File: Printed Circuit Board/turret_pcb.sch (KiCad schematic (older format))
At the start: 19 parts

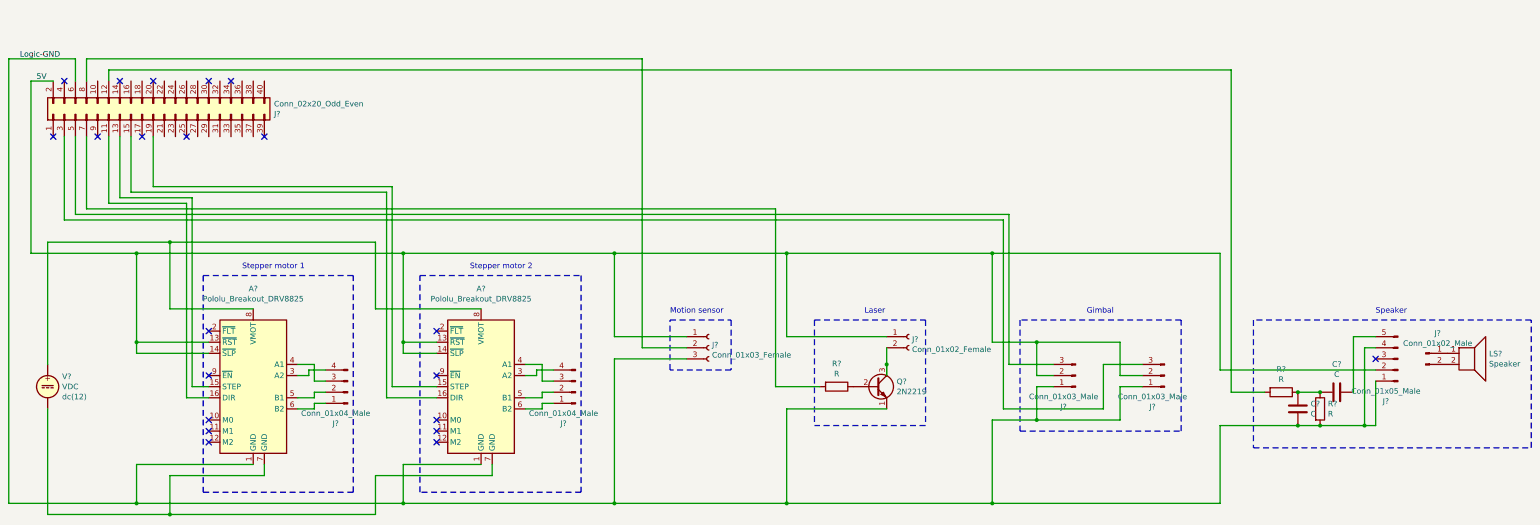
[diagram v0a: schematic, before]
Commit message: PCB separate schemas for components
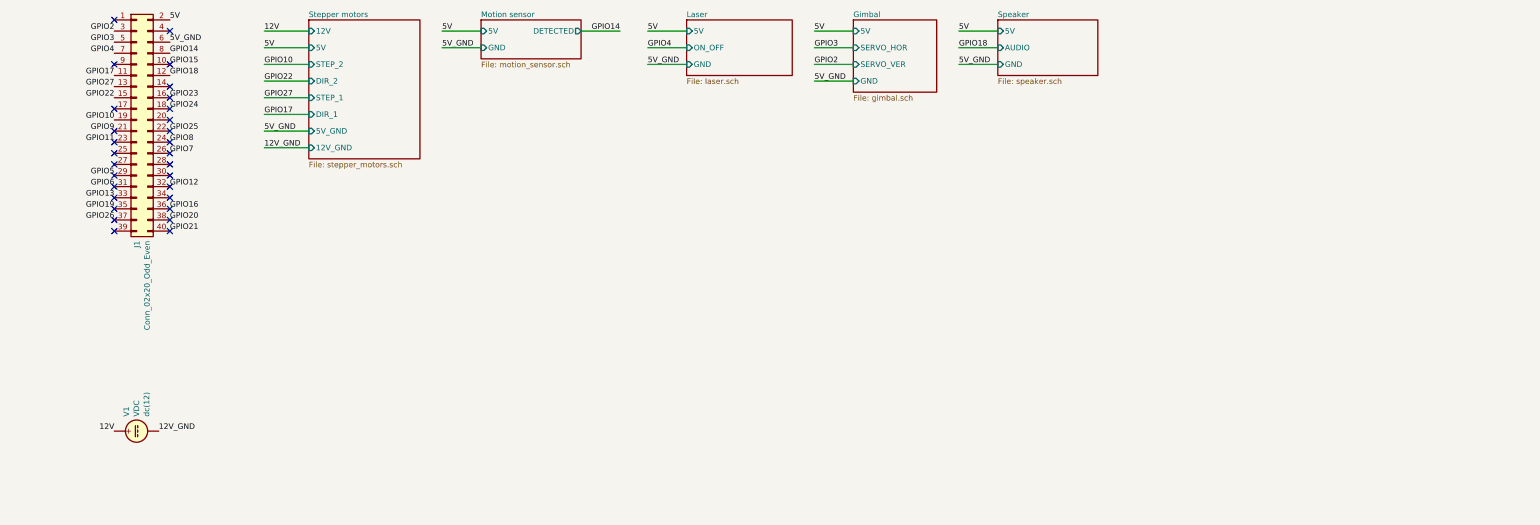
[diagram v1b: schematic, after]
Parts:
- removed A? (x2): Pololu_Breakout_DRV8825, Module:Pololu_Breakout-16_15.2x20.3mm, symbol Driver_Motor:Pololu_Breakout_DRV8825
- removed C? (x2): C, symbol Device:C
- removed J?: Conn_01x03_Female, symbol Connector:Conn_01x03_Female
- removed J? (x2): Conn_01x04_Male, symbol Connector:Conn_01x04_Male
- removed J?: Conn_01x02_Female, symbol Connector:Conn_01x02_Female
- removed J? (x2): Conn_01x03_Male, symbol Connector:Conn_01x03_Male
- removed J?: Conn_01x05_Male, symbol Connector:Conn_01x05_Male
- removed J?: Conn_01x02_Male, symbol Connector:Conn_01x02_Male
- removed LS?: Speaker, symbol Device:Speaker
- removed Q?: 2N2219, Package_TO_SOT_THT:TO-39-3, symbol Transistor_BJT:2N2219
- removed R? (x3): R, symbol Device:R
- gave numbers to parts that had none: 2
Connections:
- net GPIO27: now reaches J1.13 (Pin_13)
- net GPIO17: now reaches J1.11 (Pin_11)
- net 12V_GND: now reaches V1.2
- net 12V: now reaches V1.1
- net GPIO15: now reaches J1.10 (Pin_10)
- net GPIO18: now reaches J1.12 (Pin_12)
- net GPIO22: now reaches J1.15 (Pin_15)
- net GPIO23: now reaches J1.16 (Pin_16)
- net GPIO24: now reaches J1.18 (Pin_18)
- net GPIO10: now reaches J1.19 (Pin_19)
- net GPIO9: now reaches J1.21 (Pin_21)
- net GPIO25: now reaches J1.22 (Pin_22)
- net GPIO11: now reaches J1.23 (Pin_23)
- net GPIO8: now reaches J1.24 (Pin_24)
- net GPIO7: now reaches J1.26 (Pin_26)
- net GPIO5: now reaches J1.29 (Pin_29)
- net GPIO2: now reaches J1.3 (Pin_3)
- net GPIO6: now reaches J1.31 (Pin_31)
- net GPIO12: now reaches J1.32 (Pin_32)
- net GPIO13: now reaches J1.33 (Pin_33)
- net GPIO19: now reaches J1.35 (Pin_35)
- net GPIO16: now reaches J1.36 (Pin_36)
- net GPIO26: now reaches J1.37 (Pin_37)
- net GPIO20: now reaches J1.38 (Pin_38)
- net GPIO21: now reaches J1.40 (Pin_40)
- net GPIO3: now reaches J1.5 (Pin_5)
- net GPIO4: now reaches J1.7 (Pin_7)
- net GPIO14: now reaches J1.8 (Pin_8)
- net Logic-GND renamed 5V_GND
- no-connect marks 21 -> 29
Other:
- note removed: "Gimbal"
- note removed: "Laser"
- note removed: "Motion sensor"
- note removed: "Speaker"
- note removed: "Stepper motor 1"
- note removed: "Stepper motor 2"
- moved on the sheet: J1, V1

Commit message: PCB: physical board prototype
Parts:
- J1: footprint (none) -> Connector_PinSocket_2.54mm:PinSocket_2x20_P2.54mm_Vertical
- V1: footprint (none) -> Connector:Banana_Jack_2Pin
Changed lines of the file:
@@
 F 0 "V1" H 1830 4891 50  0000 L CNN
 F 1 "VDC" H 1830 4800 50  0000 L CNN
-F 2 "" H 1700 4800 50  0001 C CNN
+F 2 "Connector:Banana_Jack_2Pin" H 1700 4800 50  0001 C CNN
 F 3 "~" H 1700 4800 50  0001 C CNN
 F 4 "Y" H 1700 4800 50  0001 L CNN "Spice_Netlist_Enabled"
@@
 F 0 "J1" V 1704 913 50  0000 R CNN
 F 1 "Conn_02x20_Odd_Even" V 1795 913 50  0000 R CNN
-F 2 "" H 1700 2000 50  0001 C CNN
+F 2 "Connector_PinSocket_2.54mm:PinSocket_2x20_P2.54mm_Vertical" H 1700 2000 50  0001 C CNN
 F 3 "~" H 1700 2000 50  0001 C CNN
 	1    1700 2000

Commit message: PCB physical board
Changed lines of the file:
@@
 5V
 Text Label 2850 1500 0    50   ~ 0
+GPIO22
+Text Label 2850 1650 0    50   ~ 0
 GPIO10
-Text Label 2850 1650 0    50   ~ 0
-GPIO22
 Text Label 2850 1800 0    50   ~ 0
+GPIO17
+Text Label 2850 1950 0    50   ~ 0
 GPIO27
-Text Label 2850 1950 0    50   ~ 0
-GPIO17
 Text Label 2850 2100 0    50   ~ 0
 5V_GND
